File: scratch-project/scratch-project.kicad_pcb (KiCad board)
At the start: 2 copper layers, 96.5 x 96.5 mm, 5 parts

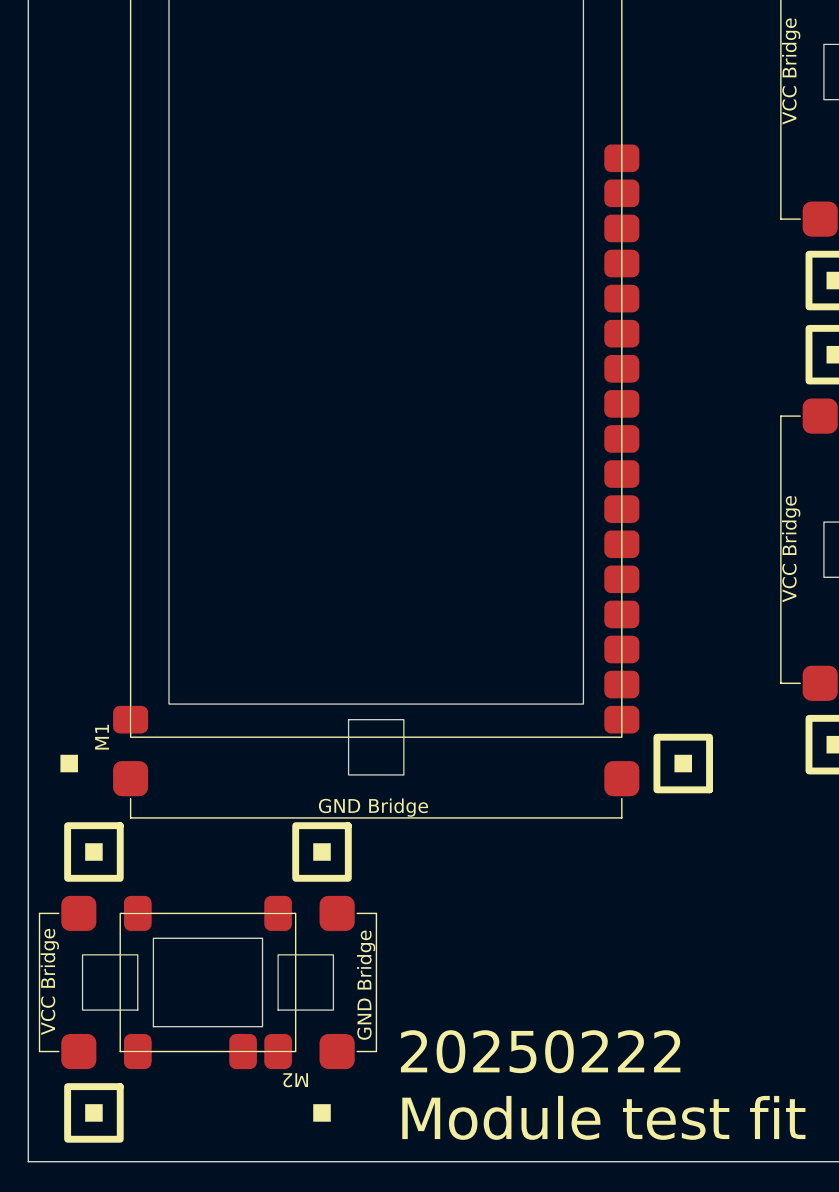
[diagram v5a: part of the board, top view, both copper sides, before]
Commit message: add low-current DC:DC regulator module
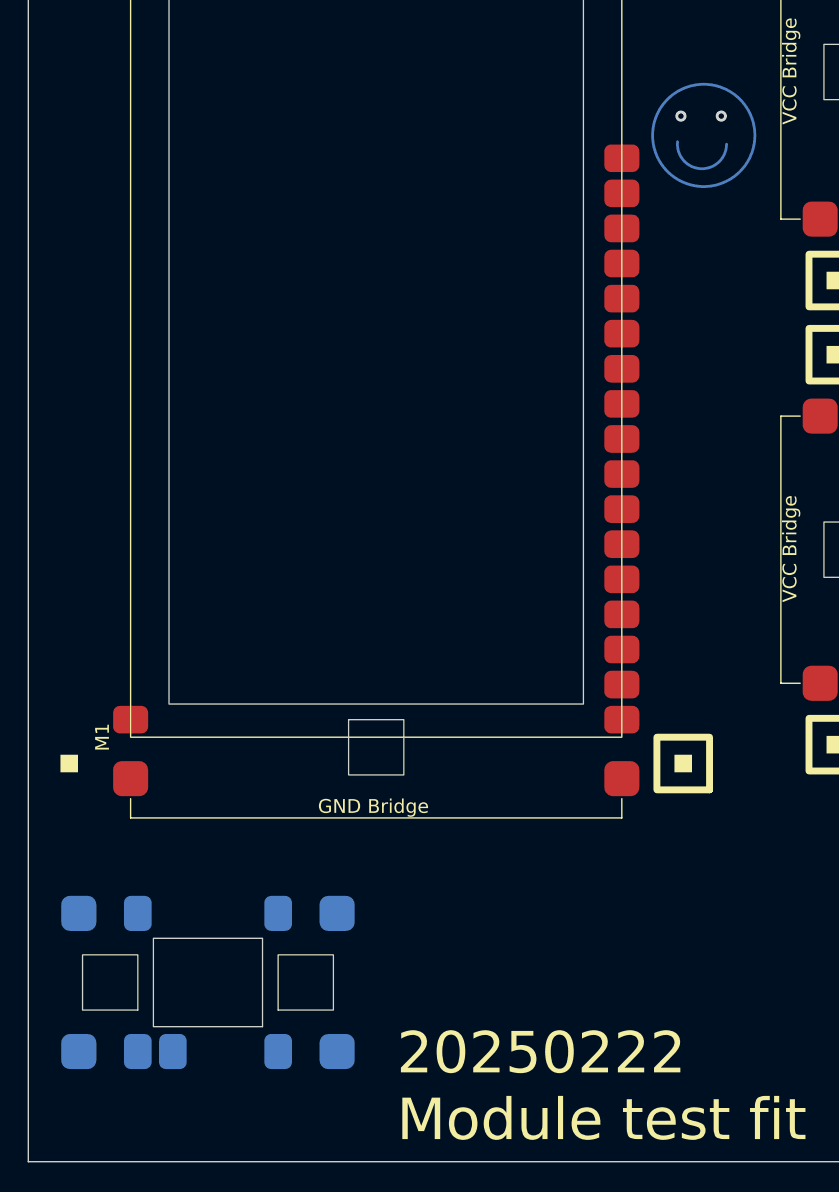
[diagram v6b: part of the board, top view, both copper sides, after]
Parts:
- M2: moved to B.Cu
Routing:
- net (no net): vias 0 -> 2
